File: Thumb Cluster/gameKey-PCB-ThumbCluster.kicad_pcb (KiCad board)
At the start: 2 copper layers, 30 x 40.2 mm, 4 parts, among them J0 Conn_01x06, J1 Conn_01x05

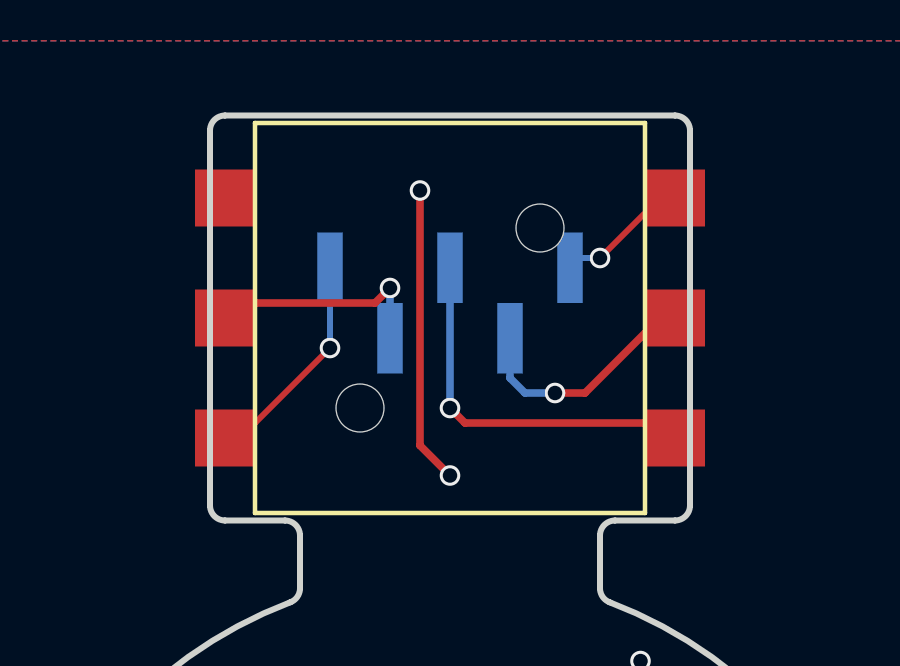
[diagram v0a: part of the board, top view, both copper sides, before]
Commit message: Critical - thumb nav switch was missing column pin Broke out away from common ground and improved labeling
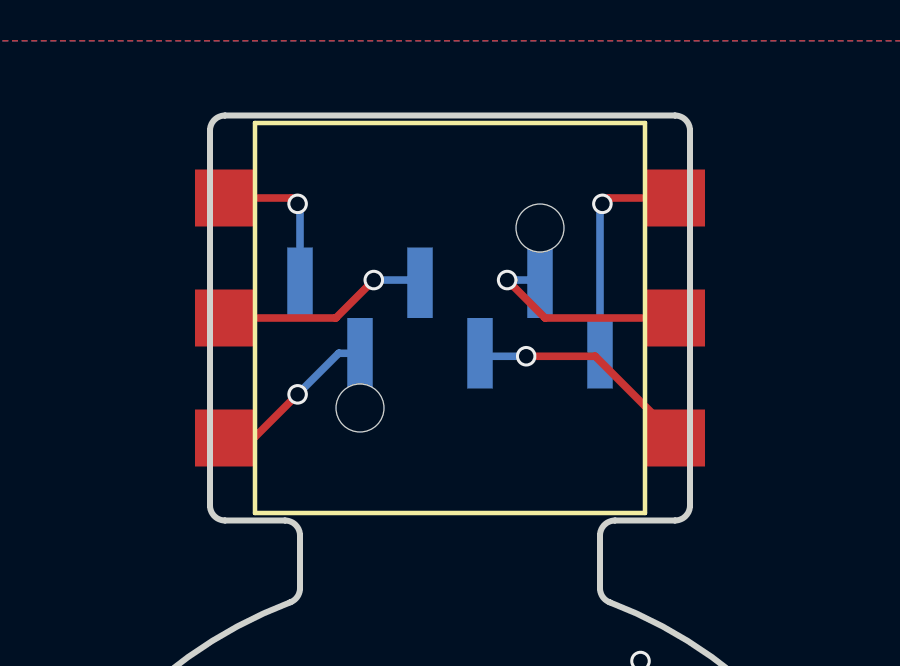
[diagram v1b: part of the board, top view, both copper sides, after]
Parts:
- removed the J1 at (0.00, -24.0)
- added J2: Conn_01x06, Connector_PinHeader_2.00mm:PinHeader_1x06_P2.00mm_Vertical_SMD_Pin1Left, B.Cu at (0.00, -23.5)
- renumbered J0 to J1, JS0 to JS1
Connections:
- NS1 pad 1: GND -> /COL
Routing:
- net GND: track 9.91 -> 0.00 mm, vias 7 -> 5
- net /COL: track 0.00 -> 5.16 mm, vias 0 -> 1
- net /NS: track 12.4 -> 7.71 mm
- net /NN: track 4.67 -> 7.51 mm
- net /NP: track 7.21 -> 5.67 mm
- net /NE: track 8.27 -> 7.25 mm
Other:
- board text added: "<C P> <W S> <E N>"
- board text removed: "P W S E N"

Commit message: Clarify thumb cluster column silkscreens
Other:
- board text added: "<C4 P> <W S> <E N>"
- board text added: "G + X Y B C5"
- board text removed: "<C P> <W S> <E N>"
- board text removed: "G + X Y B C"
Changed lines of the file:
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@@
   (gr_arc (start -11.180339 9.999999) (mid -14.573046 -3.553352) (end -5.32258 -14.023914) (layer "Edge.Cuts") (width 0.2))
   (gr_circle (center 0 0) (end 15 0) (layer "User.1") (width 0.15) (fill none))
-  (gr_text "G\n  +\nX\n  Y\nB\n  C" (at 13.335 0) (layer "B.SilkS")
+  (gr_text "G\n  +\nX\n  Y\nB\n  C5" (at 13.335 0) (layer "B.SilkS")
     (effects (font (size 1.27 1.27) (thickness 0.3048)) (justify mirror))
   )
-  (gr_text "        <C\nP>\n        <W\nS>\n        <E\nN>" (at 0 -25.4 90) (layer "B.SilkS")
+  (gr_text "        <C4\nP>\n        <W\nS>\n        <E\nN>" (at 0 -25.4 90) (layer "B.SilkS")
     (effects (font (size 1.27 1.27) (thickness 0.3048)) (justify mirror))
   )
